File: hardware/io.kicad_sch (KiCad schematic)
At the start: 43 parts, among them J1 EDGE_L, J2 EDGE_R, SW2 USER/BOOT

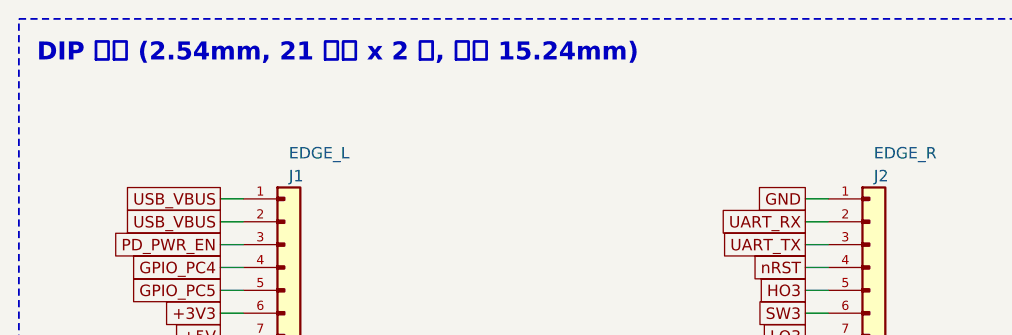
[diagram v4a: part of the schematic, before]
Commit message: 9マス版に一本化 (8マス版を削除)
- 8 マス版 (20.32mm) は JLCPCB の 2 層標準 0.127mm で配線しきれないため削除
- 9 マス版 (22.86mm, 端子列 0.7in) を hardware/ 直下・hardware/daughter/・hardware/fab/・docs/pcb/ へ移動
- ベタなし版は hardware/nopour/ (図は docs/pcb/nopour/)
- gen_pcb.py から MPB_W9 の切り替えを外し 9 マス固定に。既定ルールは 0.127mm / ビア 0.6/0.3
  (再生成した配置が確定済みの 4 基板と一致することを確認)
- 回路図の注記 (外形・列間) を 22.86mm / 17.78mm に更新し PDF を再出力
- README / stacking.md / design.md を 9 マス版のみの記述に更新

Co-Authored-By: Claude Opus 5.5 <noreply@anthropic.com>
Claude-Session: https://claude.ai/code/session_01LENFjjhDfYjJZV1NWhB9uV
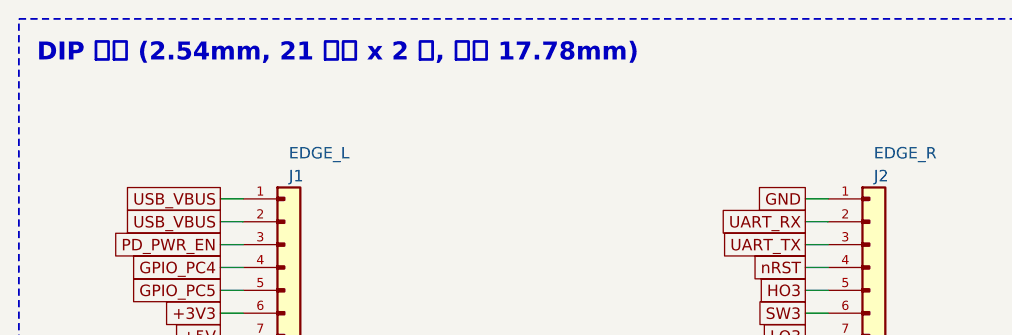
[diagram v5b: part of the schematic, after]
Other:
- note added: "DIP 端子 (2.54mm, 21 ピン x 2 列, 列間 17.78mm)"
- note removed: "DIP 端子 (2.54mm, 21 ピン x 2 列, 列間 15.24mm)"
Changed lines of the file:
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@@
 (title_block (title "mPBCH32M030DS0  CH32M030 motor-driver MCU module (DIP-42)") (date "2026-09-26") (rev "0.4") (company "ghostinkoma") (comment 1 "DIP 端子 J1/J2 / ゲート確認 LED / センシング選択 / I/O") (comment 2 "個人利用可 (クレジット表示必須) / 商用利用は要連絡 / 無保証  -  LICENSE 参照"))
 (rectangle (start 15 20) (end 150 285) (stroke (width 0.2) (type dash)) (fill (type none)))
-(text "DIP 端子 (2.54mm, 21 ピン x 2 列, 列間 15.24mm)" (exclude_from_sim no) (at 17 25 0) (effects (font (size 2 2) (thickness 0.3) (bold yes)) (justify left bottom)))
+(text "DIP 端子 (2.54mm, 21 ピン x 2 列, 列間 17.78mm)" (exclude_from_sim no) (at 17 25 0) (effects (font (size 2 2) (thickness 0.3) (bold yes)) (justify left bottom)))
 (rectangle (start 160 20) (end 405 110) (stroke (width 0.2) (type dash)) (fill (type none)))
 (text "ゲート確認 LED (モジュール上面に 8 個: 子基板の部品面はヒートシンク側で見えないため)" (exclude_from_sim no) (at 162 25 0) (effects (font (size 2 2) (thickness 0.3) (bold yes)) (justify left bottom)))

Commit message: モジュールの nFAULT フィルタ・USB GND 強化, 3D モデルと干渉チェック, 電流容量チェックの道具
- nFAULT (TIM1 BKIN) に 1nF (C120) を追加。470Ω と 0.47µs。CH32M030 の TIM1 には BKIN の
  デジタルフィルタが無いため, ハードの RC で誤停止を防ぐ (配線済みの基板へ追加して迷路配線で接続)
- USB-C (J8) の GND パッド脇に GND ビアを追加し, 下面の GND ベタへ直結 (5A 帰路の細い箇所を解消)
- USB-PD の要求電流を min(want_mA, 3000mA) に頭打ち (J8 の VBUS パッド口元の銅幅で決まる上限)
- KiCad 8 標準に無い 3D モデルを作成 (QFN48 0.35mm, TSON Advance, 1812 / NANO2 ヒューズ)
  tools/gen_3dmodels.py, 割当は gen_pcb.py models
- tools/check_3d.py: STEP で部品どうしの干渉, モジュールを子基板へ挿した状態, ヒートシンク面の高さを確認
- tools/power_check/: 銅箔の抵抗網で電流分布を解き IPC-2221 と比較 / 3.3V 系のノイズ結合の確認
- 下面の部品高さの記述を実測 (3D) の 1.65mm に訂正

Co-Authored-By: Claude Opus 5.5 <noreply@anthropic.com>
Claude-Session: https://claude.ai/code/session_01LENFjjhDfYjJZV1NWhB9uV
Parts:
- added R110: 10k (DNP), Resistor_SMD:R_0402_1005Metric, symbol mdrv:R
- C103: renamed from R110; value 10k (DNP) -> 0.1uF/50V; footprint Resistor_SMD:R_0402_1005Metric -> Capacitor_SMD:C_0402_1005Metric; symbol mdrv:R -> mdrv:C; MPN (none) -> Murata GRM155R71H104KE14D (X7R 1005); now fitted
- C120: renamed from C103; value 0.1uF/50V -> 1nF/50V; MPN Murata GRM155R71H104KE14D (X7R 1005) -> Murata GRM155R71H102KA01D (X7R 1005)
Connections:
- net +3V3: now also R110.1; no longer C103.1
- net GND: now also C103.2
- net NTC: now also C103.1, R110.2; no longer C103.2, C120.1
- net nFAULT: now also C120.1
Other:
- moved on the sheet: C120
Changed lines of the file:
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@@
 (wire (pts (xy 380 243.81) (xy 380 246.35)) (stroke (width 0) (type default)))
 (global_label "nFAULT" (shape passive) (at 380 246.35 270) (fields_autoplaced yes) (effects (font (size 1.27 1.27)) (justify right)) (property "Intersheetrefs" "${INTERSHEET_REFS}" (at 380 246.35 0) (effects (font (size 1.27 1.27)) (hide yes))))
+(symbol (lib_id "mdrv:C") (at 398 252 90) (unit 1) (exclude_from_sim no) (in_bom yes) (on_board yes) (dnp no)
+(property "Reference" "C120" (at 398 249.2 90) (effects (font (size 1.27 1.27))))
+(property "Value" "1nF/50V" (at 398 255.6 90) (effects (font (size 1.27 1.27))))
+(property "Footprint" "Capacitor_SMD:C_0402_1005Metric" (at 398 252 0) (effects (font (size 1.27 1.27)) (hide yes)))
+(property "Datasheet" "~" (at 398 252 0) (effects (font (size 1.27 1.27)) (hide yes)))
+(property "MPN" "Murata GRM155R71H102KA01D (X7R 1005)" (at 398 252 0) (effects (font (size 1.27 1.27)) (hide yes)))
+(pin "1")
+(pin "2")
+(instances (project "mPBCH32M030DS0" (path "/87b4cdf7-ae48-57cd-a772-8ad5802448bf/ee5b2127-6dad-5c0a-8011-aab5e1b930bd" (reference "C120") (unit 1))))
+)
+(wire (pts (xy 394.19 252) (xy 391.65 252)) (stroke (width 0) (type default)))
+(global_label "nFAULT" (shape passive) (at 391.65 252 180) (fields_autoplaced yes) (effects (font (size 1.27 1.27)) (justify right)) (property "Intersheetrefs" "${INTERSHEET_REFS}" (at 391.65 252 0) (effects (font (size 1.27 1.27)) (hide yes))))
+(wire (pts (xy 401.81 252) (xy 404.35 252)) (stroke (width 0) (type default)))
+(global_label "GND" (shape passive) (at 404.35 252 0) (fields_autoplaced yes) (effects (font (size 1.27 1.27)) (justify left)) (property "Intersheetrefs" "${INTERSHEET_REFS}" (at 404.35 252 0) (effects (font (size 1.27 1.27)) (hide yes))))
 (symbol (lib_id "mdrv:C") (at 350 262 0) (unit 1) (exclude_from_sim no) (in_bom yes) (on_board yes) (dnp no)
 (property "Reference" "C103" (at 352.54 260.73 0) (effects (font (size 1.27 1.27)) (justify left)))
